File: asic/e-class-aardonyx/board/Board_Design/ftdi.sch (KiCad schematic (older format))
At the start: 60 parts, among them J1 USB_B_6PIN, J17 USB_OTG, J18 Conn_1x3_M, J2 Conn_1x8, J3 Conn_1x3_M, U1 FT2232H, U16 93LC56BT-I_OT, Y1 12MHz

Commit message: Added few components
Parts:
- added FB6, FB7: 47E,FB,0402, Inductor_SMD:L_0402_1005Metric, symbol Aardonyx-rescue:Ferrite_Bead_Small-aardonyx
- R52: Description RES SMD 10K OHM 1% 1/8W 0805 -> RES 10K OHM 5% 1/8W 0402; Digikey PartNumber 311-10.0KCRCT-ND -> 2019-SG73S1ETTP103JCT-ND; Manufactured Part Number RC0805FR-0710KL -> SG73S1ETTP103J; Maufaturer Yageo -> KOA Speer Electronics, Inc.
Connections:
- net GNDREF: now also FB6.2, FB7.1; no longer J1.5 (SHLD1), J1.6 (SHLD2), J17.6 (SHLD1), J17.7 (SHLD2), J17.8 (SHLD3), J17.9 (SHLD4)
- new net: FB7.2, J17.6 (SHLD1), J17.7 (SHLD2), J17.8 (SHLD3), J17.9 (SHLD4)
- new net: FB6.1, J1.5 (SHLD1), J1.6 (SHLD2)
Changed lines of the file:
@@
 Wire Wire Line
 	1100 3750 900  3750
-Connection ~ 900  3750
-Wire Wire Line
-	900  3750 900  3850
 Wire Wire Line
 	1100 3850 900  3850
-Connection ~ 900  3850
 $Comp
 L Aardonyx-rescue:GND-aardonyx #PWR049
@@
 Wire Wire Line
 	1550 850  1550 950
-$Comp
-L Aardonyx-rescue:GND-aardonyx #PWR02
-U 1 1 5F1918CD
-P 1000 2700
-F 0 "#PWR02" H 1000 2450 50  0001 C CNN
-F 1 "GND" H 1005 2527 50  0000 C CNN
-F 2 "" H 1000 2700 50  0001 C CNN
-F 3 "" H 1000 2700 50  0001 C CNN
-	1    1000 2700
-	1    0    0    -1
-$EndComp
 Wire Wire Line
 	1000 2200 1000 2350
 Wire Wire Line
-	1450 2000 1500 2000
-Wire Wire Line
-	1500 2000 1500 2350
-Wire Wire Line
-	1500 2350 1100 2350
-Connection ~ 1000 2350
-Wire Wire Line
-	1000 2350 1000 2700
+	1700 2000 1700 2350
 Wire Wire Line
 	1100 2200 1100 2350
-Connection ~ 1100 2350
 Wire Wire Line
 	1100 2350 1000 2350
@@
 F 1 "10KE,0402" V 8100 5800 50  0000 L CNN
 F 2 "Resistor_SMD:R_0402_1005Metric" V 8240 5940 50  0001 C CNN
-F 3 "https://www.digikey.in/product-detail/en/yageo/RC0805FR-0710KL/311-10-0KCRCT-ND/730482" H 8200 5950 50  0001 C CNN
+F 3 "https://www.digikey.in/product-detail/en/koa-speer-electronics-inc/SG73S1ETTP103J/2019-SG73S1ETTP103JCT-ND/10280218" H 8200 5950 50  0001 C CNN
 F 4 "NA" H 8300 5800 50  0000 C CNN "Field4"
-F 5 "RES SMD 10K OHM 1% 1/8W 0805" H 8200 5950 50  0001 C CNN "Description"
-F 6 "311-10.0KCRCT-ND" H 8200 5950 50  0001 C CNN "Digikey PartNumber"
-F 7 "RC0805FR-0710KL" H 8200 5950 50  0001 C CNN "Manufactured Part Number"
-F 8 "Yageo" H 8200 5950 50  0001 C CNN "Maufaturer"
+F 5 "RES 10K OHM 5% 1/8W 0402" H 8200 5950 50  0001 C CNN "Description"
+F 6 "2019-SG73S1ETTP103JCT-ND" H 8200 5950 50  0001 C CNN "Digikey PartNumber"
+F 7 "SG73S1ETTP103J" H 8200 5950 50  0001 C CNN "Manufactured Part Number"
+F 8 "KOA Speer Electronics, Inc." H 8200 5950 50  0001 C CNN "Maufaturer"
 	1    8200 5950
 	1    0    0    -1
@@
 Wire Wire Line
 	10150 5350 10150 5650
+$Comp
+L Aardonyx-rescue:Ferrite_Bead_Small-aardonyx FB7
+U 1 1 5EF1A57F
+P 800 3750
+F 0 "FB7" V 700 3850 50  0000 C CNN
+F 1 "47E,FB,0402" V 900 3750 50  0000 C CNN
+F 2 "Inductor_SMD:L_0402_1005Metric" V 730 3750 50  0001 C CNN
+F 3 "https://www.digikey.in/product-detail/en/w%C3%BCrth-elektronik/742792608/732-1596-1-ND/1639540" H 800 3750 50  0001 C CNN
+F 4 "FERRITE BEAD 47 OHM 0603 1LN" H 800 3750 50  0001 C CNN "Description"
+F 5 "732-1596-1-ND" H 800 3750 50  0001 C CNN "Digikey PartNumber"
+F 6 "742792608" H 800 3750 50  0001 C CNN "Manufactured Part Number"
+F 7 "Wurth Elektronik" H 800 3750 50  0001 C CNN "Maufaturer"
+	1    800  3750
+	0    -1   -1   0
+$EndComp
+Connection ~ 1100 2350
+$Comp
+L Aardonyx-rescue:Ferrite_Bead_Small-aardonyx FB6
+U 1 1 5EF19677
+P 1500 2350
+F 0 "FB6" H 1400 2250 50  0000 C CNN
+F 1 "47E,FB,0402" V 1600 2350 50  0000 C CNN
+F 2 "Inductor_SMD:L_0402_1005Metric" V 1430 2350 50  0001 C CNN
+F 3 "https://www.digikey.in/product-detail/en/w%C3%BCrth-elektronik/742792608/732-1596-1-ND/1639540" H 1500 2350 50  0001 C CNN
+F 4 "FERRITE BEAD 47 OHM 0603 1LN" H 1500 2350 50  0001 C CNN "Description"
+F 5 "732-1596-1-ND" H 1500 2350 50  0001 C CNN "Digikey PartNumber"
+F 6 "742792608" H 1500 2350 50  0001 C CNN "Manufactured Part Number"
+F 7 "Wurth Elektronik" H 1500 2350 50  0001 C CNN "Maufaturer"
+	1    1500 2350
+	0    -1   -1   0
+$EndComp
+Wire Wire Line
+	1100 2350 1400 2350
+Wire Wire Line
+	1450 2000 1700 2000
+Wire Wire Line
+	1600 2350 1700 2350
+Connection ~ 900  3750
+$Comp
+L Aardonyx-rescue:GND-aardonyx #PWR0168
+U 1 1 5EFC7B53
+P 700 3750
+F 0 "#PWR0168" H 700 3500 50  0001 C CNN
+F 1 "GND" H 705 3577 50  0000 C CNN
+F 2 "" H 700 3750 50  0001 C CNN
+F 3 "" H 700 3750 50  0001 C CNN
+	1    700  3750
+	0    1    1    0
+$EndComp
+$Comp
+L Aardonyx-rescue:GND-aardonyx #PWR0173
+U 1 1 5EFEBA59
+P 1700 2700
+F 0 "#PWR0173" H 1700 2450 50  0001 C CNN
+F 1 "GND" H 1705 2527 50  0000 C CNN
+F 2 "" H 1700 2700 50  0001 C CNN
+F 3 "" H 1700 2700 50  0001 C CNN
+	1    1700 2700
+	1    0    0    -1
+$EndComp
+Wire Wire Line
+	1700 2350 1700 2700
+Connection ~ 1700 2350
 $EndSCHEMATC

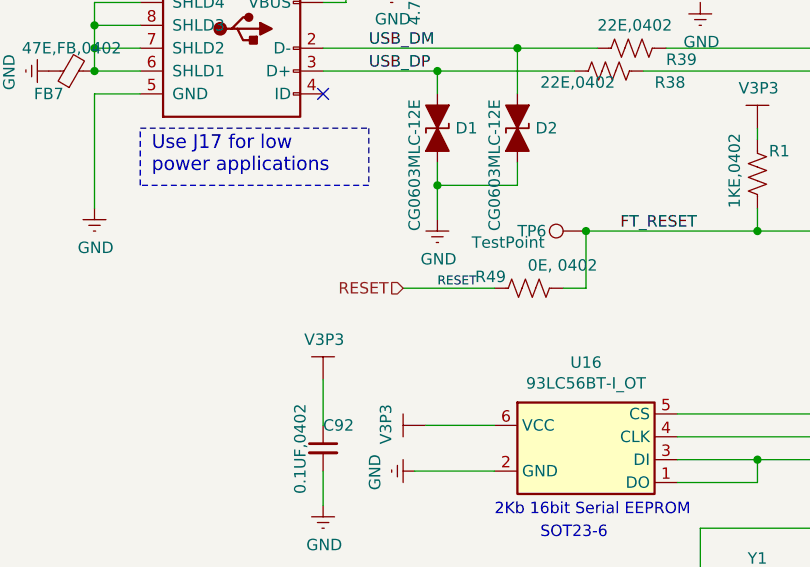
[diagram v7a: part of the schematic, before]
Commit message: Replacing ADM1085 with ADM1186
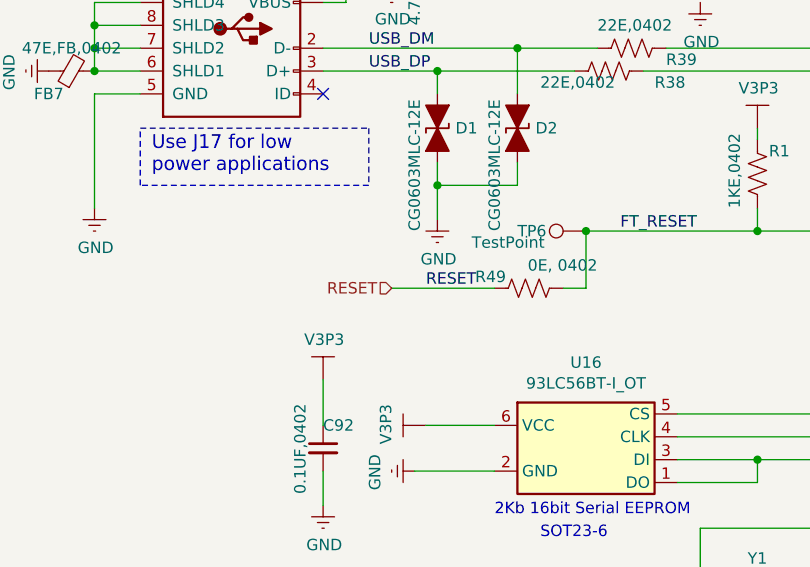
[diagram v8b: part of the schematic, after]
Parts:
- R1: Description RES SMD 1K OHM 5% 1/10W 0402 -> RES SMD 1K OHM 5% 1/10W 0402
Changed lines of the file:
@@
 F 2 "Resistor_SMD:R_0402_1005Metric" V 3840 4190 50  0001 C CNN
 F 3 "https://www.digikey.in/product-detail/en/panasonic-electronic-components/ERJ-2GEJ102X/P1-0KJCT-ND/146897" H 3800 4200 50  0001 C CNN
-F 4 "RES SMD 1K OHM 5% 1/10W 0402 " H 3800 4200 50  0001 C CNN "Description"
+F 4 "RES SMD 1K OHM 5% 1/10W 0402" H 3800 4200 50  0001 C CNN "Description"
 F 5 "P1.0KJCT-ND " H 3800 4200 50  0001 C CNN "Digikey PartNumber"
 F 6 "ERJ-2GEJ102X " H 3800 4200 50  0001 C CNN "Manufactured Part Number"
@@
 	0    -1   -1   0
 $EndComp
-$Comp
-L Aardonyx-rescue:R_US-aardonyx R49
-U 1 1 5F59FAB5
-P 2800 4700
-F 0 "R49" V 2850 4800 50  0000 L CNN
-F 1 "0E, 0402" V 2900 4400 50  0000 L CNN
-F 2 "Resistor_SMD:R_0402_1005Metric" V 2840 4690 50  0001 C CNN
-F 3 "https://www.digikey.in/product-detail/en/vishay-dale/CRCW04020000Z0ED/541-0-0JCT-ND/1182611" H 2800 4700 50  0001 C CNN
-F 4 "RES SMD 0 OHM JUMPER 1/16W 0402" H 2800 4700 50  0001 C CNN "Description"
-F 5 "541-0.0JCT-ND" H 2800 4700 50  0001 C CNN "Digikey PartNumber"
-F 6 "CRCW04020000Z0ED" H 2800 4700 50  0001 C CNN "Manufactured Part Number"
-F 7 "Vishay Dale" H 2800 4700 50  0001 C CNN "Maufaturer"
-	1    2800 4700
-	0    -1   -1   0
-$EndComp
 Wire Wire Line
 	2950 4700 3050 4700
@@
 	3050 4450 3800 4450
 Connection ~ 3050 4450
-Wire Wire Line
-	2250 4700 2650 4700
-Text Label 2400 4700 0    39   ~ 0
-RESET
-Text HLabel 2250 4700 0    50   Input ~ 0
+Text HLabel 2200 4700 0    50   Input ~ 0
 RESET
 Text Notes 750  3100 0    60   ~ 0
@@
 	1700 2350 1700 2700
 Connection ~ 1700 2350
+Wire Wire Line
+	2200 4700 2650 4700
+$Comp
+L Aardonyx-rescue:R_US-aardonyx R49
+U 1 1 5F59FAB5
+P 2800 4700
+F 0 "R49" V 2850 4800 50  0000 L CNN
+F 1 "0E, 0402" V 2900 4400 50  0000 L CNN
+F 2 "Resistor_SMD:R_0402_1005Metric" V 2840 4690 50  0001 C CNN
+F 3 "https://www.digikey.in/product-detail/en/vishay-dale/CRCW04020000Z0ED/541-0-0JCT-ND/1182611" H 2800 4700 50  0001 C CNN
+F 4 "RES SMD 0 OHM JUMPER 1/16W 0402" H 2800 4700 50  0001 C CNN "Description"
+F 5 "541-0.0JCT-ND" H 2800 4700 50  0001 C CNN "Digikey PartNumber"
+F 6 "CRCW04020000Z0ED" H 2800 4700 50  0001 C CNN "Manufactured Part Number"
+F 7 "Vishay Dale" H 2800 4700 50  0001 C CNN "Maufaturer"
+	1    2800 4700
+	0    -1   -1   0
+$EndComp
+Text Label 2350 4700 0    50   ~ 0
+RESET
 $EndSCHEMATC
